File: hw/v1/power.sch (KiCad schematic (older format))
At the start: 24 parts, among them J502 USB_C_Receptacle, J601 Screw_Terminal, J602 USB_B_Micro, Q604 Q_PMOS_GSD, Q605 Q_PMOS_GSD, U602 FUSB302BMPX

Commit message: Progress...
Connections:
- net GND: no longer J601.1 (Pin_1), R626.2
- new net GNDPWR: J601.1 (Pin_1), R626.2
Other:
- note added: "DNP resistors and use\nMCU's internal pull-ups?"
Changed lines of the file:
@@
 	7800 5350 7800 5300
-$Comp
-L power:GND #PWR?
-U 1 1 5F585E6C
-P 7800 5350
-AR Path="/5F585E6C" Ref="#PWR?"  Part="1"
-AR Path="/5F017F08/5F585E6C" Ref="#PWR0144"  Part="1"
-F 0 "#PWR0144" H 7800 5100 50  0001 C CNN
-F 1 "GND" H 7805 5177 50  0000 C CNN
-F 2 "" H 7800 5350 50  0001 C CNN
-F 3 "" H 7800 5350 50  0001 C CNN
-	1    7800 5350
-	-1   0    0    -1
-$EndComp
 $Comp
 L Connector:Screw_Terminal_01x02 J?
@@
 $EndComp
 $Comp
-L power:GND #PWR?
-U 1 1 5F980B77
-P 8250 5900
-AR Path="/5F980B77" Ref="#PWR?"  Part="1"
-AR Path="/5F017F08/5F980B77" Ref="#PWR0157"  Part="1"
-F 0 "#PWR0157" H 8250 5650 50  0001 C CNN
-F 1 "GND" H 8255 5727 50  0000 C CNN
-F 2 "" H 8250 5900 50  0001 C CNN
-F 3 "" H 8250 5900 50  0001 C CNN
-	1    8250 5900
-	-1   0    0    -1
-$EndComp
-$Comp
 L Device:D_Zener D606
 U 1 1 5F981156
@@
 	9750 4050 9200 4050
 Connection ~ 9200 4050
+Text Notes 6800 2600 0    50   ~ 0
+DNP resistors and use\nMCU's internal pull-ups?
+$Comp
+L power:GNDPWR #PWR?
+U 1 1 5F17DF79
+P 7800 5350
+F 0 "#PWR?" H 7800 5150 50  0001 C CNN
+F 1 "GNDPWR" H 7804 5196 50  0000 C CNN
+F 2 "" H 7800 5300 50  0001 C CNN
+F 3 "" H 7800 5300 50  0001 C CNN
+	1    7800 5350
+	1    0    0    -1
+$EndComp
+$Comp
+L power:GNDPWR #PWR?
+U 1 1 5F17E19E
+P 8250 5900
+F 0 "#PWR?" H 8250 5700 50  0001 C CNN
+F 1 "GNDPWR" H 8254 5746 50  0000 C CNN
+F 2 "" H 8250 5850 50  0001 C CNN
+F 3 "" H 8250 5850 50  0001 C CNN
+	1    8250 5900
+	1    0    0    -1
+$EndComp
 $EndSCHEMATC

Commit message: Soon...
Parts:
- added C615, C616: 100n, Capacitor_SMD:C_0603_1608Metric, symbol Device:C
- added R627, R628: 100k, Resistor_SMD:R_0603_1608Metric, symbol Device:R
- added R629: 22k, Resistor_SMD:R_0603_1608Metric, symbol Device:R
- added R630: 100, Resistor_SMD:R_0603_1608Metric, symbol Device:R
- D606: footprint (none) -> Diode_SMD:D_SOD-123
- Q604, Q605: value Q_PMOS_GSD -> ZVN4206G; footprint (none) -> Package_TO_SOT_SMD:SOT-223-3_TabPin2
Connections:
- net CHARGE_POWER: now also Q604.3 (D), Q605.3 (D), C616.1; no longer Q604.2 (S), Q605.2 (S)
- net GND: now also C615.2, R627.2; no longer J502.A1 (GND), J502.A12 (GND), J502.B1 (GND), J502.B12 (GND), J502.S1 (SHIELD)
- net GNDPWR: now also J502.A1 (GND), J502.A12 (GND), J502.B1 (GND), J502.B12 (GND)
- net USB_VBUS: now also Q604.2 (S), R628.1; no longer Q604.3 (D)
- net at J601.2 (Pin_2): now also Q605.2 (S); no longer Q605.3 (D)
- net at Q604.1 (G): now also R628.2, R629.1, R630.2
- new net: C616.2, R630.1
- new net EN_POWER: R629.2
- new net SHIELD: C615.1, J502.S1 (SHIELD), R627.1
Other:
- note added: "Block the return current\nfrom going in the shield."
- note added: "TODO: ESD protection?"
- moved on the sheet: C609, C610, C611, C612, C613, C614, D604, D605, D606, J502, J601, Q604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

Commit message: Soooooon...
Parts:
- removed C615: 100n, Capacitor_SMD:C_0603_1608Metric, symbol Device:C
- removed R627: 100k, Resistor_SMD:R_0603_1608Metric, symbol Device:R
- added J3: Conn_01x02, Connector_JST:JST_EH_S2B-EH_1x02_P2.50mm_Horizontal, symbol Connector_Generic:Conn_01x02
- added Q15: Q_NMOS_GSD, Package_TO_SOT_SMD:SOT-23, symbol Device:Q_NMOS_GSD
- added R108, R109: 100, Resistor_SMD:R_0603_1608Metric, symbol Device:R
- renumbered C609 to C37, C610 to C38, C616 to C39, C612 to C40, C613 to C41, C611 to C42, C614 to C43, D604 to D13, D605 to D14, D606 to D15, D608 to D16, J502 to J1, J601 to J2, J602 to J4, Q604 to Q13, Q605 to Q14, R620 to R101, R621 to R102, R622 to R103, R628 to R104, R630 to R105, R629 to R106, R626 to R107, R625 to R110, R623 to R111, R624 to R112, TP601 to TP1, U602 to U9
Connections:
- net CHARGE_POWER: now also J3.1 (Pin_1)
- net GND: now also R109.1; no longer J4.6 (Shield)
- net GNDPWR: now also Q15.2 (S)
- new net: J3.2 (Pin_2), Q15.3 (D)
- new net: Q15.1 (G), R108.1
- new net EN_FAN: R108.2, R109.2
- new net SHIELD2: J4.6 (Shield)
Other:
- note added: "Charge power switch"
- note added: "DC connector"
- note added: "Fan connector"
- note added: "Micro-USB for data"
- note added: "USB-C for power\nand data"
- moved on the sheet: C37, C38, C39, C40, C41, C42, C43, D13, D14, D15, J1, J2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

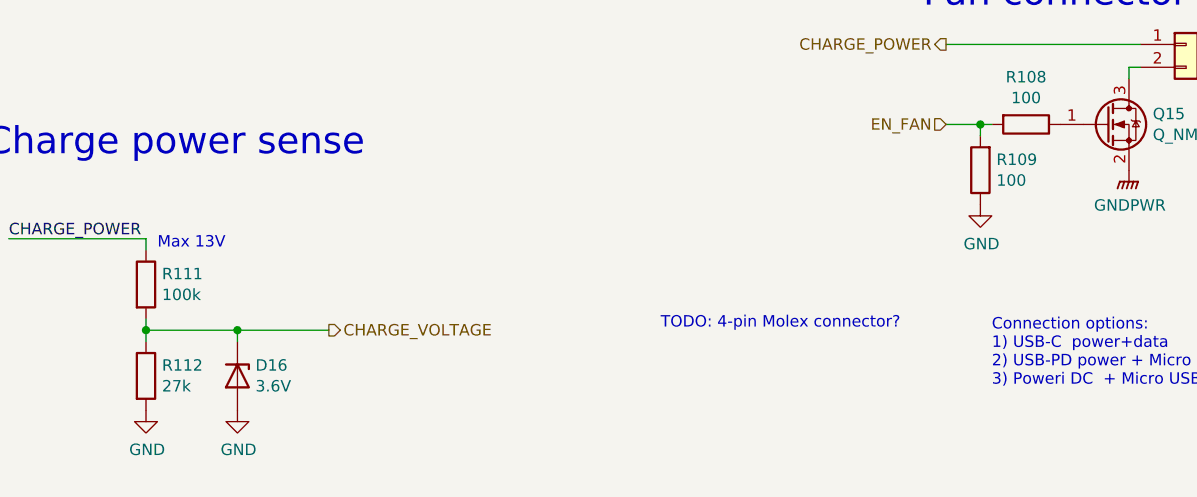
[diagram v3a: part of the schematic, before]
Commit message: Layout done and MCU pins rearranged
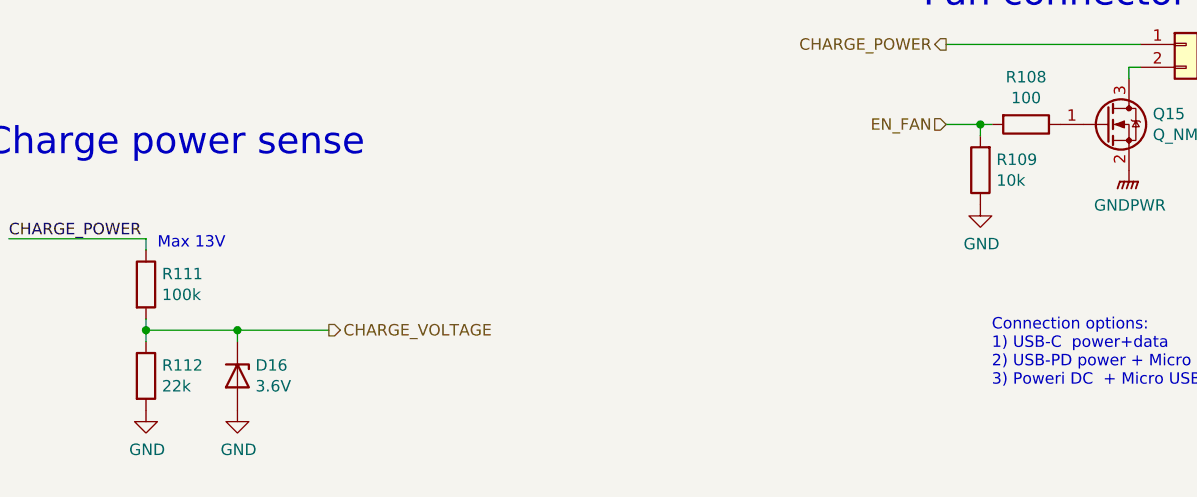
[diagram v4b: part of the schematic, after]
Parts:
- R109: value 100 -> 10k
- R112: value 27k -> 22k
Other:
- note removed: "TODO: 4-pin Molex connector?"
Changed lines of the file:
@@
 Sheet 6 7
 Title "Cell Shaper: Power"
-Date ""
+Date "2020-07-15"
 Rev "v1"
 Comp "petrinm"
@@
 Wire Wire Line
 	5950 2200 5950 2500
-Text Notes 8150 6700 2    50   ~ 0
-TODO: 4-pin Molex connector?
 $Comp
 L power:GND #PWR?
@@
 AR Path="/5F017F08/5F5927E8" Ref="R112"  Part="1"
 F 0 "R112" H 4920 6946 50  0000 L CNN
-F 1 "27k" H 4920 6855 50  0000 L CNN
+F 1 "22k" H 4920 6855 50  0000 L CNN
 F 2 "Resistor_SMD:R_0603_1608Metric" V 4780 6900 50  0001 C CNN
 F 3 "~" H 4850 6900 50  0001 C CNN
@@
 AR Path="/5F017F08/5F568799" Ref="R109"  Part="1"
 F 0 "R109" H 8430 5954 50  0000 R CNN
-F 1 "100" H 8430 6045 50  0000 R CNN
+F 1 "10k" H 8430 6045 50  0000 R CNN
 F 2 "Resistor_SMD:R_0603_1608Metric" V 8430 6000 50  0001 C CNN
 F 3 "~" H 8500 6000 50  0001 C CNN
